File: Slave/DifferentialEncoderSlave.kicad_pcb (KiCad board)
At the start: 4 copper layers, 52.5 x 36.5 mm, 21 parts, among them J1 RJ45_Shielded, U1 SN75C1167, U2 MA730, U3 LDFM33PVR

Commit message: Export master BOM
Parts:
- H5, H6: footprint MountingHole:MountingHole_3mm -> MountingHole:MountingHole_3.2mm_M3_DIN965
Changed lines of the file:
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@@
-(kicad_pcb (version 20171130) (host pcbnew "(5.1.7)-1")
+(kicad_pcb (version 20171130) (host pcbnew "(5.1.8)-1")
   (general
     (thickness 1.6)
-    (drawings 25)
+    (drawings 22)
     (tracks 133)
     (zones 0)
@@
     (add_net "Net-(R2-Pad1)")
   )
+  (module MountingHole:MountingHole_3.2mm_M3_DIN965 (layer F.Cu)
+    (at 145.0125 68)
+    (descr "Mounting Hole 3.2mm, no annular, M3, DIN965")
+    (tags "mounting hole 3.2mm no annular m3 din965")
+    (attr virtual)
+    (fp_text reference H6 (at -2.5125 -3.5) (layer F.SilkS) hide
+      (effects (font (size 1 1) (thickness 0.15)))
+    )
+    (fp_text value MountingHole (at 0 3.8) (layer F.Fab)
+      (effects (font (size 1 1) (thickness 0.15)))
+    )
+    (fp_circle (center 0 0) (end 3.05 0) (layer F.CrtYd) (width 0.05))
+    (fp_circle (center 0 0) (end 2.8 0) (layer Cmts.User) (width 0.15))
+    (fp_text user %R (at 0.3 0) (layer F.Fab)
+      (effects (font (size 1 1) (thickness 0.15)))
+    )
+    (pad 1 np_thru_hole circle (at 0 0) (size 3.2 3.2) (drill 3.2) (layers *.Cu *.Mask))
+  )
+  (module MountingHole:MountingHole_3.2mm_M3_DIN965 (layer F.Cu)
+    (at 98.9875 68)
+    (descr "Mounting Hole 3.2mm, no annular, M3, DIN965")
+    (tags "mounting hole 3.2mm no annular m3 din965")
+    (attr virtual)
+    (fp_text reference H5 (at 2.5125 -3.5) (layer F.SilkS) hide
+      (effects (font (size 1 1) (thickness 0.15)))
+    )
+    (fp_text value MountingHole (at 0 3.8) (layer F.Fab)
+      (effects (font (size 1 1) (thickness 0.15)))
+    )
+    (fp_circle (center 0 0) (end 3.05 0) (layer F.CrtYd) (width 0.05))
+    (fp_circle (center 0 0) (end 2.8 0) (layer Cmts.User) (width 0.15))
+    (fp_text user %R (at 0.3 0) (layer F.Fab)
+      (effects (font (size 1 1) (thickness 0.15)))
+    )
+    (pad 1 np_thru_hole circle (at 0 0) (size 3.2 3.2) (drill 3.2) (layers *.Cu *.Mask))
+  )
   (module Wetmelon:RJLSE4118101 (layer F.Cu)
     (at 122.025 79.75)
@@
       (rotate (xyz -90 0 0))
     )
-  )
-  (module MountingHole:MountingHole_3mm (layer F.Cu)
-    (at 145.0125 68)
-    (descr "Mounting Hole 3mm, no annular")
-    (tags "mounting hole 3mm no annular")
-    (attr virtual)
-    (fp_text reference H6 (at -3.0125 -3.5) (layer F.SilkS) hide
-      (effects (font (size 1 1) (thickness 0.15)))
-    )
-    (fp_text value MountingHole (at 0 4) (layer F.Fab)
-      (effects (font (size 1 1) (thickness 0.15)))
-    )
-    (fp_circle (center 0 0) (end 3.25 0) (layer F.CrtYd) (width 0.05))
-    (fp_circle (center 0 0) (end 3 0) (layer Cmts.User) (width 0.15))
-    (fp_text user %R (at 0.3 0) (layer F.Fab)
-      (effects (font (size 1 1) (thickness 0.15)))
-    )
-    (pad 1 np_thru_hole circle (at 0 0) (size 3 3) (drill 3) (layers *.Cu *.Mask))
-  )
-  (module MountingHole:MountingHole_3mm (layer F.Cu)
-    (at 98.9875 68)
-    (descr "Mounting Hole 3mm, no annular")
-    (tags "mounting hole 3mm no annular")
-    (attr virtual)
-    (fp_text reference H5 (at 3.5125 -3.5) (layer F.SilkS) hide
-      (effects (font (size 1 1) (thickness 0.15)))
-    )
-    (fp_text value MountingHole (at 0 4) (layer F.Fab)
-      (effects (font (size 1 1) (thickness 0.15)))
-    )
-    (fp_circle (center 0 0) (end 3.25 0) (layer F.CrtYd) (width 0.05))
-    (fp_circle (center 0 0) (end 3 0) (layer Cmts.User) (width 0.15))
-    (fp_text user %R (at 0.3 0) (layer F.Fab)
-      (effects (font (size 1 1) (thickness 0.15)))
-    )
-    (pad 1 np_thru_hole circle (at 0 0) (size 3 3) (drill 3) (layers *.Cu *.Mask))
   )
   (module MountingHole:MountingHole_3mm (layer F.Cu)
@@
     )
   )
-  (dimension 52.525 (width 0.12) (layer F.SilkS)
-    (gr_text "52.525 mm" (at 122 52.73) (layer F.SilkS)
-      (effects (font (size 1 1) (thickness 0.15)))
-    )
-    (feature1 (pts (xy 148.2625 68) (xy 148.2625 53.413579)))
-    (feature2 (pts (xy 95.7375 68) (xy 95.7375 53.413579)))
-    (crossbar (pts (xy 95.7375 54) (xy 148.2625 54)))
-    (arrow1a (pts (xy 148.2625 54) (xy 147.135996 54.586421)))
-    (arrow1b (pts (xy 148.2625 54) (xy 147.135996 53.413579)))
-    (arrow2a (pts (xy 95.7375 54) (xy 96.864004 54.586421)))
-    (arrow2b (pts (xy 95.7375 54) (xy 96.864004 53.413579)))
-  )
-  (dimension 28.77 (width 0.12) (layer F.SilkS)
-    (gr_text "28.770 mm" (at 122 102.269999) (layer F.SilkS)
-      (effects (font (size 1 1) (thickness 0.15)))
-    )
-    (feature1 (pts (xy 136.385 97.5) (xy 136.385 101.58642)))
-    (feature2 (pts (xy 107.615 97.5) (xy 107.615 101.58642)))
-    (crossbar (pts (xy 107.615 100.999999) (xy 136.385 100.999999)))
-    (arrow1a (pts (xy 136.385 100.999999) (xy 135.258496 101.58642)))
-    (arrow1b (pts (xy 136.385 100.999999) (xy 135.258496 100.413578)))
-    (arrow2a (pts (xy 107.615 100.999999) (xy 108.741504 101.58642)))
-    (arrow2b (pts (xy 107.615 100.999999) (xy 108.741504 100.413578)))
-  )
-  (dimension 36.5 (width 0.12) (layer F.SilkS)
-    (gr_text "36.500 mm" (at 153.77 79.25 270) (layer F.SilkS)
-      (effects (font (size 1 1) (thickness 0.15)))
-    )
-    (feature1 (pts (xy 136.5 97.5) (xy 153.086421 97.5)))
-    (feature2 (pts (xy 136.5 61) (xy 153.086421 61)))
-    (crossbar (pts (xy 152.5 61) (xy 152.5 97.5)))
-    (arrow1a (pts (xy 152.5 97.5) (xy 151.913579 96.373496)))
-    (arrow1b (pts (xy 152.5 97.5) (xy 153.086421 96.373496)))
-    (arrow2a (pts (xy 152.5 61) (xy 151.913579 62.126504)))
-    (arrow2b (pts (xy 152.5 61) (xy 153.086421 62.126504)))
-  )
   (gr_arc (start 106.23 76) (end 107.615 76) (angle -65) (layer Edge.Cuts) (width 0.05))

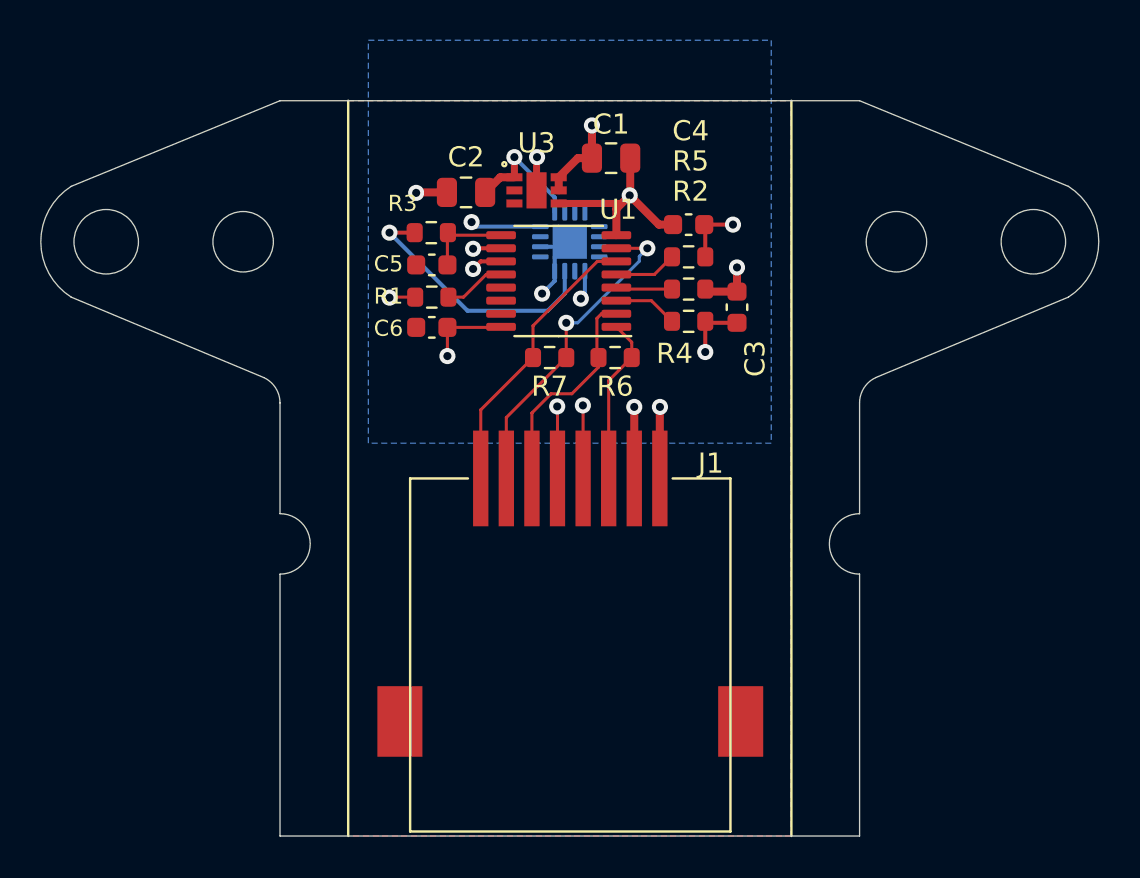
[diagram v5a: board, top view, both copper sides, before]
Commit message: Make the encoder 1.3mm shorter to make it flush with the case
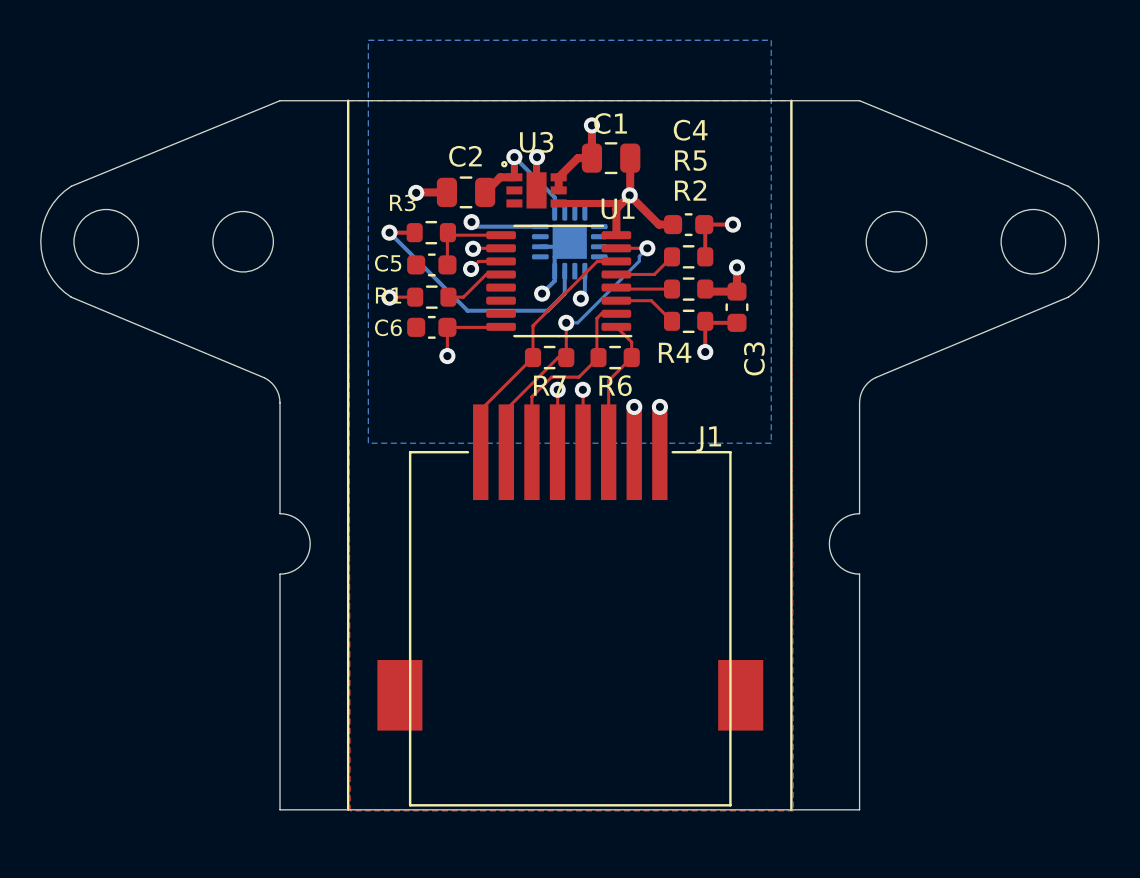
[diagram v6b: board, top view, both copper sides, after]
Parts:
- moved J1 1.30 mm to (122.0, 78.5)
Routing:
- net /MISO+: track 15.1 -> 13.8 mm
- net /MISO-: track 13.7 -> 12.5 mm
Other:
- board size 52.5 x 36.5 mm -> 52.5 x 35.2 mm

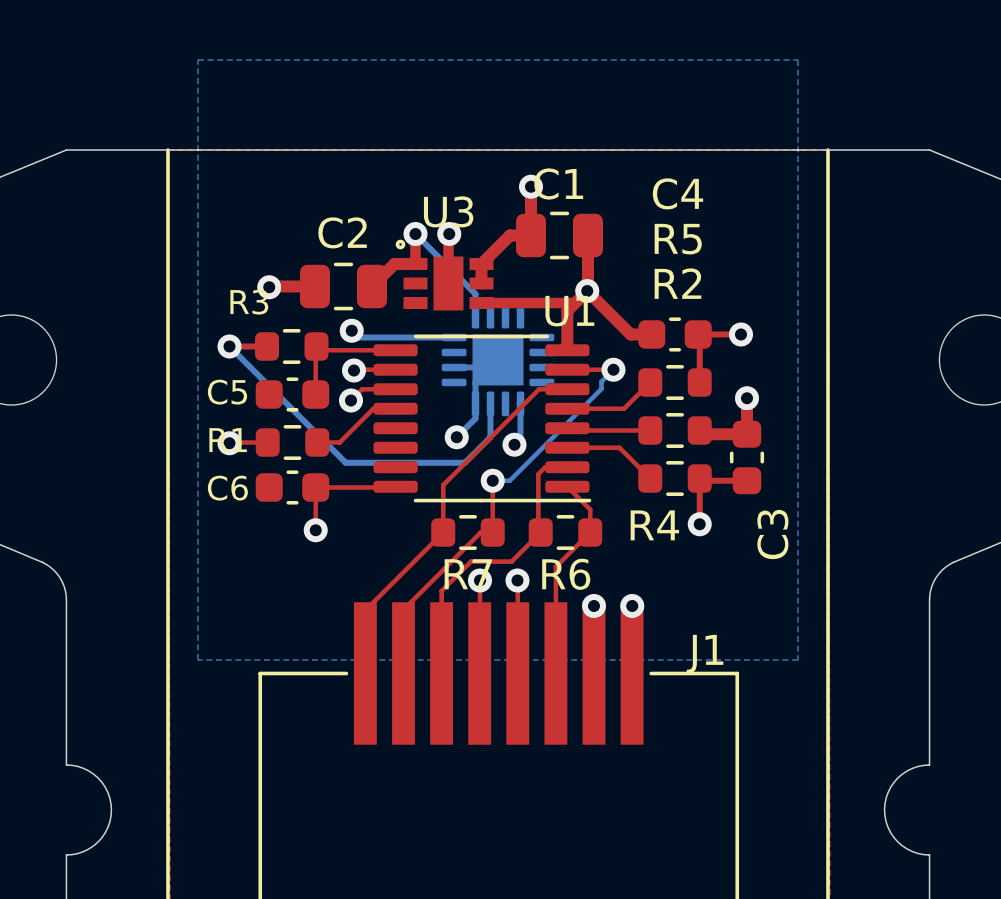
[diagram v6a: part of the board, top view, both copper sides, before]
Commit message: Encoder side TSSOP -> SOP 5.3x6.2
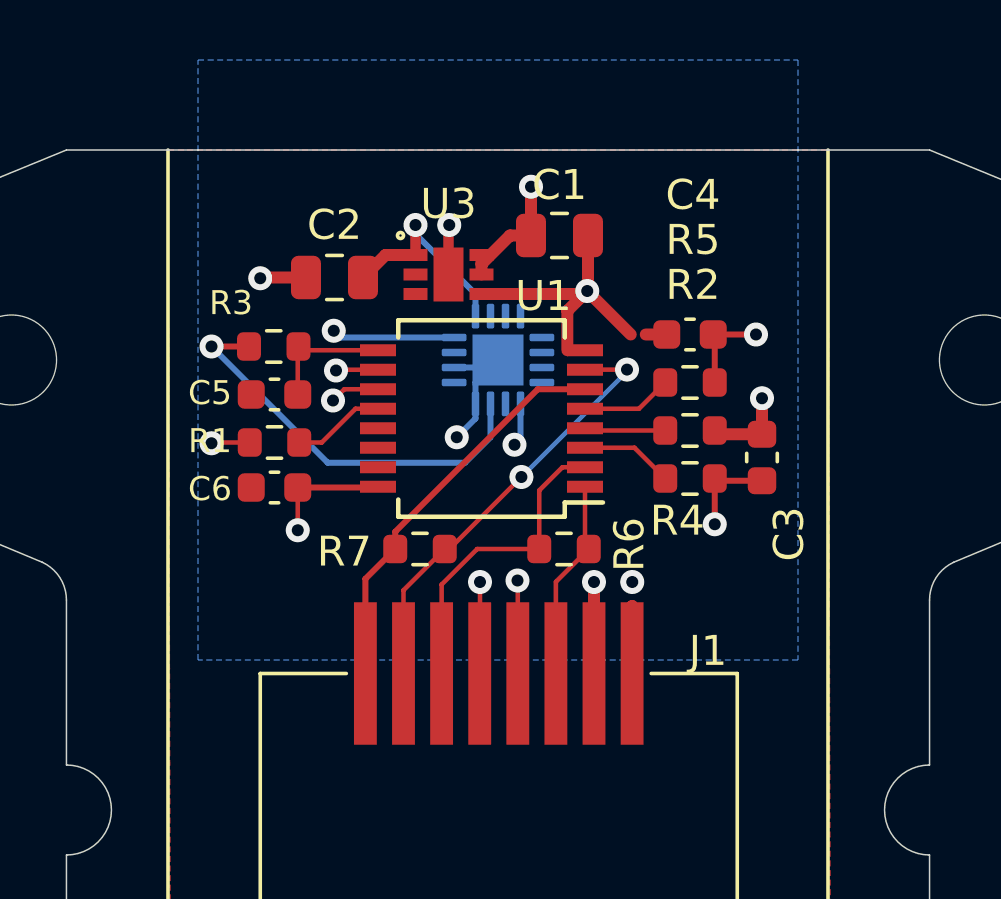
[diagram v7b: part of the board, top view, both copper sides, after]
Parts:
- U1: footprint Package_SO:TSSOP-16_4.4x5mm_P0.65mm -> Package_SO:SSOP-16_5.3x6.2mm_P0.65mm
- moved R7 1.69 mm to (119.4, 74.3)
- moved C5 0.60 mm to (114.5, 69.2)
- moved C6 0.60 mm to (114.5, 72.2)
- moved R1 0.60 mm to (114.5, 70.8)
- moved R3 0.60 mm to (114.5, 67.5)
- moved R6 0.55 mm to (124.2, 74.3)
- moved C3 0.50 mm to (130.8, 71.2)
- moved C4 0.50 mm to (128.4, 67.2)
- moved R2 0.50 mm to (128.4, 70.3)
- moved R4 0.50 mm to (128.4, 72.0)
- moved R5 0.50 mm to (128.4, 68.8)
- moved C2 0.42 mm to (116.5, 65.2)
- moved U3 0.30 mm to (120.3, 65.2)
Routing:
- net /CSn-: track 16.4 -> 14.7 mm
- net /CLK: track 22.2 -> 23.9 mm
- net /CLK-: track 8.32 -> 6.73 mm
- net +5V: track 13.3 -> 14.1 mm
- net /CLK+: track 11.2 -> 10.5 mm
- net /CSn+: track 14.1 -> 13.4 mm
- net /MISO+: track 13.8 -> 14.4 mm
- net /MISO: track 13.0 -> 13.6 mm
- net /MISO-: track 12.5 -> 13.1 mm

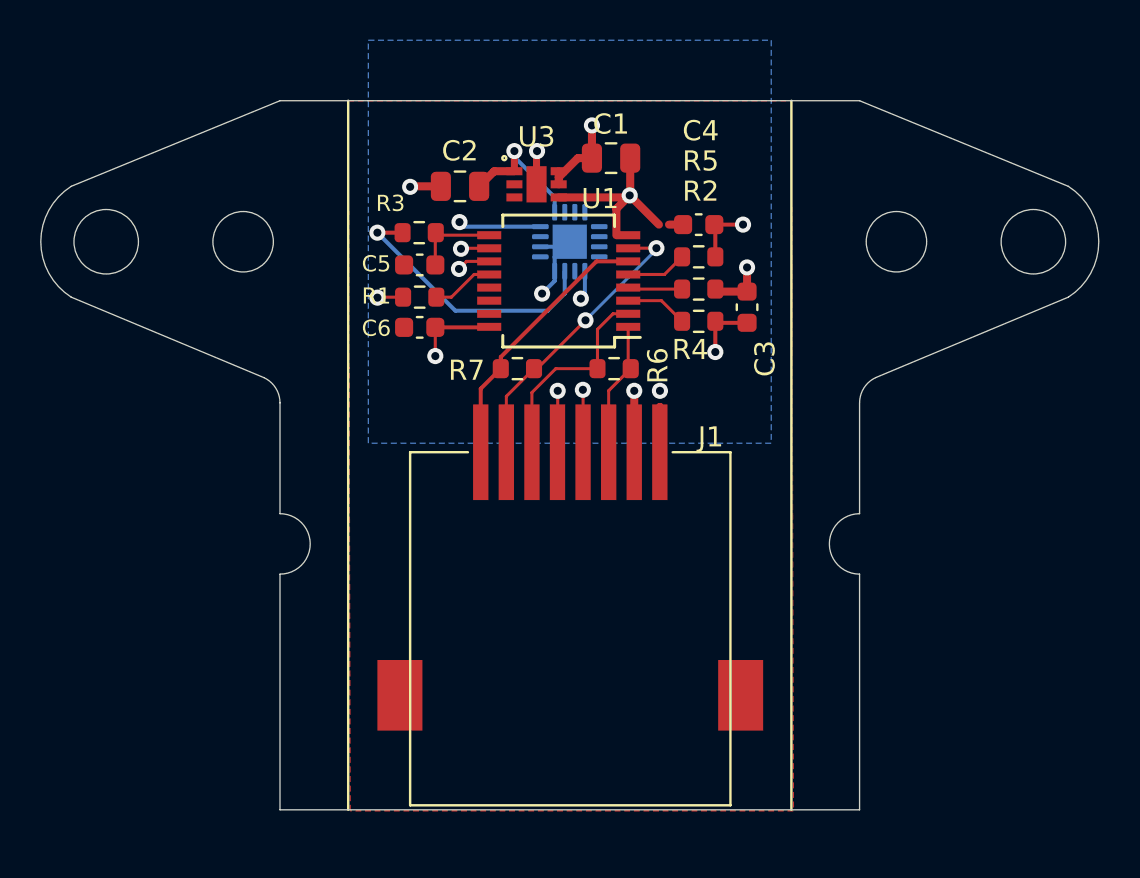
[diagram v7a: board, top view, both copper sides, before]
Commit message: Start RS485 revision
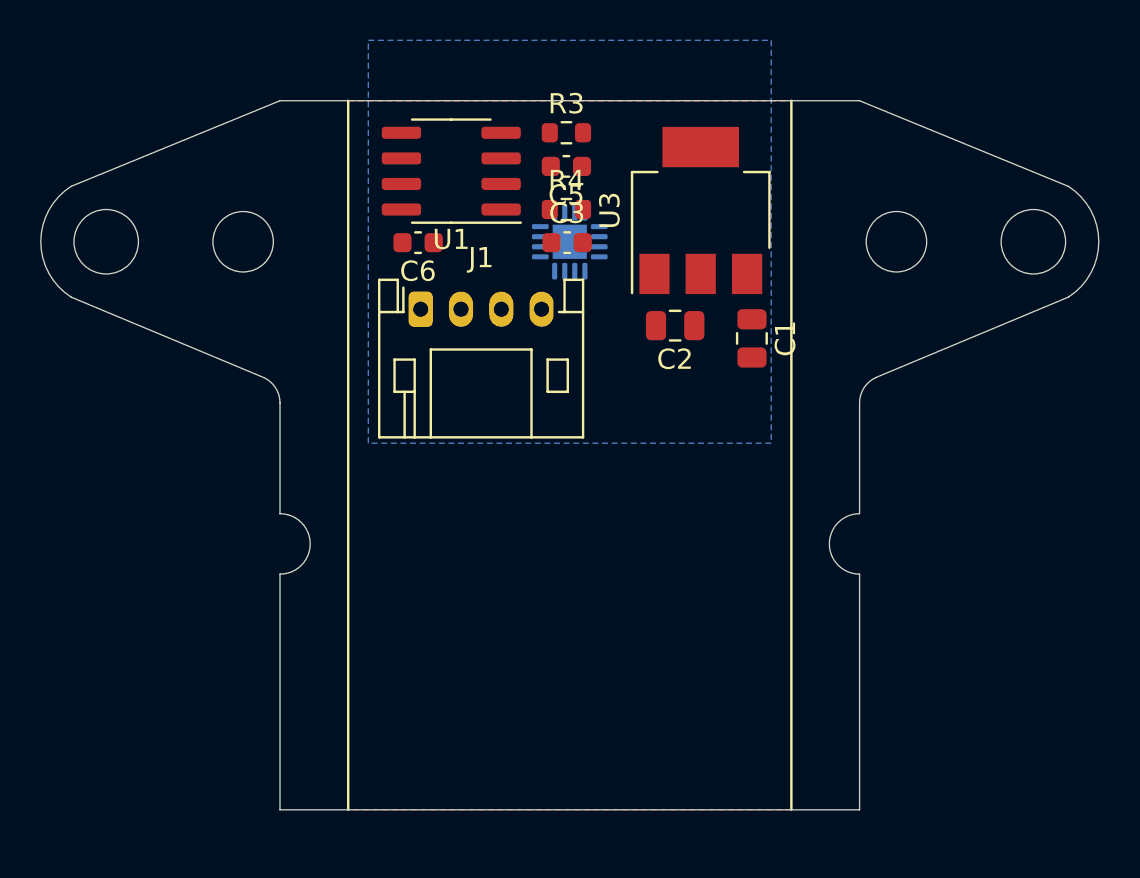
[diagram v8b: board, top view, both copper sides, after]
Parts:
- removed C4: 22pF, Capacitor_SMD:C_0603_1608Metric
- removed R1, R2: 1k, Resistor_SMD:R_0603_1608Metric
- removed R5: 680, Resistor_SMD:R_0603_1608Metric
- removed R6, R7: 100, Resistor_SMD:R_0603_1608Metric
- C1: value 1uF -> 22uF
- C2: value 4.7uF -> 22uF
- J1: value RJ45_Shielded -> Conn_01x04; footprint Wetmelon:RJLSE4118101 -> Connector_JST:JST_PH_S4B-PH-K_1x04_P2.00mm_Horizontal
- U1: value SN75C1167 -> LTC2850xS8; footprint Package_SO:SSOP-16_5.3x6.2mm_P0.65mm -> Package_SO:SOIC-8_3.9x4.9mm_P1.27mm
- U3: value LDFM33PVR -> AZ1117-3.3; footprint Wetmelon:DFN6-2x2 -> Package_TO_SOT_SMD:SOT-223-3_TabPin2
- moved C2 12.7 mm to (127.2, 72.2)
- moved C1 11.4 mm to (131.0, 72.8), turned to -90 degrees
- moved J1 10.3 mm to (114.6, 71.3)
- moved C3 9.49 mm to (121.9, 68.0), turned to 0 degrees
- moved R3 8.83 mm to (121.8, 62.6), turned to 0 degrees
- moved C5 8.77 mm to (121.8, 64.3), turned to 180 degrees
- moved R4 8.60 mm to (121.8, 66.4)
- moved U3 8.25 mm to (128.5, 66.5), turned to 90 degrees
- moved U1 7.63 mm to (116.1, 64.5)
- moved C6 4.21 mm to (114.5, 68.0), turned to 180 degrees
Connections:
- net /CSn+ renamed /RS485_A
- net /CSn- renamed /RS485_B
- C3 pad 2: /CLK -> /UART_RX
- C5 pad 2: /MISO_2D -> /DI
- J1 pad 3: /CLK+ -> +5V
- J1 pad 4: /MISO- -> GNDD
- R3 pad 1: /MISO_2D -> /DI
- R3 pad 2: /MISO -> /UART_TX
- R4 pad 1: /CLK_1R -> /RO
- R4 pad 2: /CLK -> /UART_RX
- U1 pad 1: /CLK- -> /RO
- U1 pad 2: /CLK+ -> /~{RE}
- U1 pad 3: /CLK_1R -> /DE
- U1 pad 4: Net-(R2-Pad1) -> /DI
- U1 pad 5: /CSn_2R -> GNDD
- U1 pad 8: GNDD -> +5V
- U2 pad 1: (no net) -> unconnected-(U2-Pad1)
- U2 pad 11: (no net) -> unconnected-(U2-Pad11)
- U2 pad 14: (no net) -> unconnected-(U2-Pad14)
- U2 pad 15: (no net) -> unconnected-(U2-Pad15)
- U2 pad 16: (no net) -> unconnected-(U2-Pad16)
- U2 pad 2: (no net) -> unconnected-(U2-Pad2)
- U2 pad 3: (no net) -> unconnected-(U2-Pad3)
- U2 pad 4: (no net) -> unconnected-(U2-Pad4)
- U2 pad 6: (no net) -> unconnected-(U2-Pad6)
- U2 pad 9: (no net) -> unconnected-(U2-Pad9)
- U3 pad 1: +3V3 -> GNDD
- U3 pad 2: (no net) -> +3V3
- U3 pad 3: (no net) -> +5V
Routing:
- net GNDD: track 25.3 -> 0.00 mm, vias 6 -> 0
- net /CLK: track 23.9 -> 0.00 mm, vias 2 -> 0
- net /RS485_B: track 14.7 -> 0.00 mm, vias 2 -> 0
- net /MISO+: track 14.4 -> 0.00 mm, vias 2 -> 0
- net +5V: track 14.1 -> 0.00 mm, vias 4 -> 0
- net /CSn: track 14.1 -> 0.00 mm, vias 2 -> 0
- net /MISO: track 13.6 -> 0.00 mm, vias 1 -> 0
- net /RS485_A: track 13.4 -> 0.00 mm
- net /MISO-: track 13.1 -> 0.00 mm, vias 2 -> 0
- net /CLK+: track 10.5 -> 0.00 mm
- net /CLK-: track 6.73 -> 0.00 mm
- net +3V3: track 6.63 -> 0.00 mm, vias 1 -> 0
- net /MISO_2D: track 4.31 -> 0.00 mm
- net /CLK_1R: track 3.10 -> 0.00 mm
- net Net-(R1-Pad2): track 3.09 -> 0.00 mm
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- added copper zone on F.Cu, net +3V3
- removed copper zone on F.Cu, net GNDD
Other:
- outline, holes or cut-outs redrawn
- net class Default removed
